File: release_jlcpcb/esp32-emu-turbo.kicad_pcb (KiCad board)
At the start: 4 copper layers, 160 x 75 mm, 71 parts, among them J1 USB-C-16P, J3 JST-PH-2P, J4 FPC-40P-0.5mm, SW1 SW-SMD-5.1x5.1, SW10 SW-SMD-5.1x5.1, SW11 SW-SMD-5.1x5.1, SW12 SW-SMD-5.1x5.1, SW13 SW-SMD-5.1x5.1, SW2 SW-SMD-5.1x5.1, SW3 SW-SMD-5.1x5.1, SW4 SW-SMD-5.1x5.1, SW5 SW-SMD-5.1x5.1, SW6 SW-SMD-5.1x5.1, SW7 SW-SMD-5.1x5.1, SW8 SW-SMD-5.1x5.1, SW9 SW-SMD-5.1x5.1, U1 ESP32-S3-WROOM-1-N16R8, U2 ESOP-8, U3 SOT-223, U5 SOP-16, U6 TF-01A

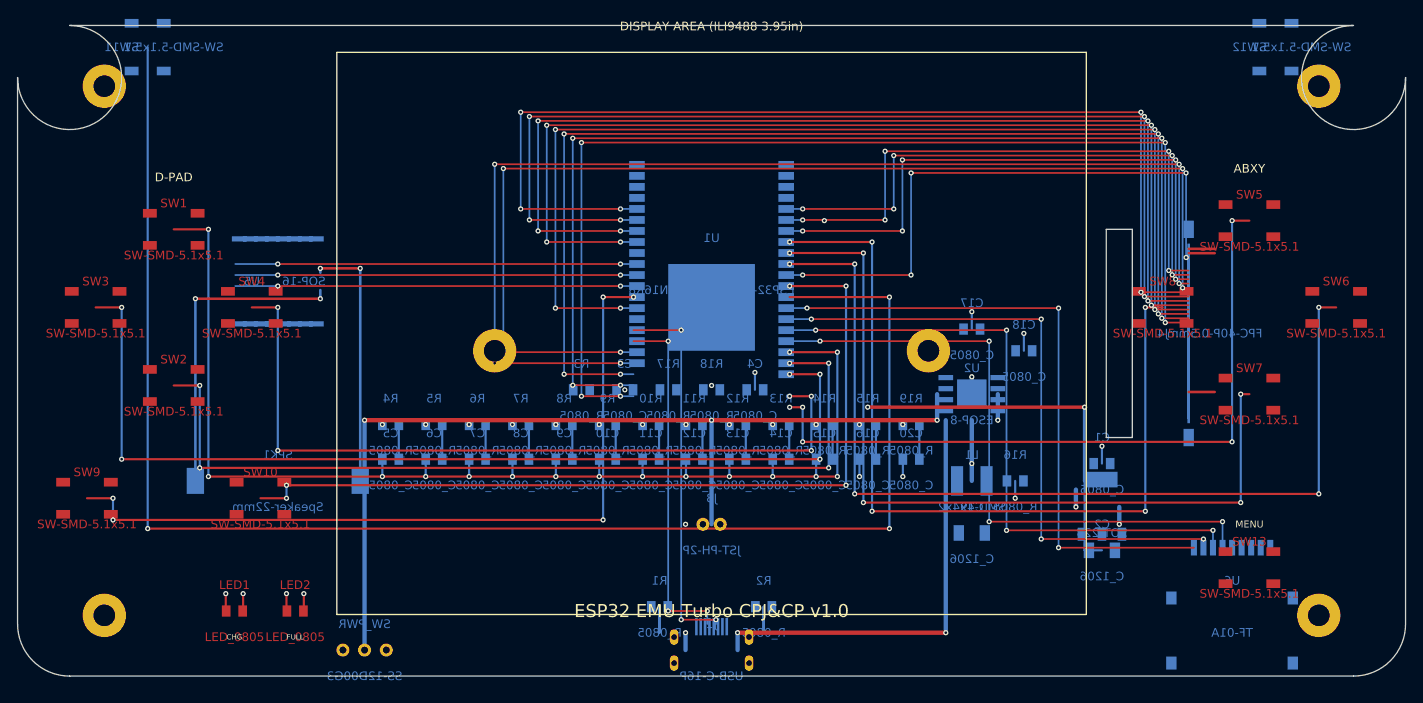
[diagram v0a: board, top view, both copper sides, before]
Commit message: Fix text on copper layers, add DRC check, regenerate JLCPCB files
- Move all Reference/Value text from F.Cu/B.Cu to F.SilkS/B.SilkS
  in PCB generator (board.py) — fixes 130 text-on-copper issues
- Add "Text on Copper Layers" check to drc_check.py (blocks commit
  if any property text is placed on copper layers)
- Regenerate Gerbers, CPL, and gerbers.zip with KiCad 10 (nightly)
- Re-render all 4 PCB 3D views + GLB + 2D SVGs with corrected layers
- Update release_jlcpcb/ folder with fresh exports

Co-Authored-By: Claude Opus 4.6 <noreply@anthropic.com>
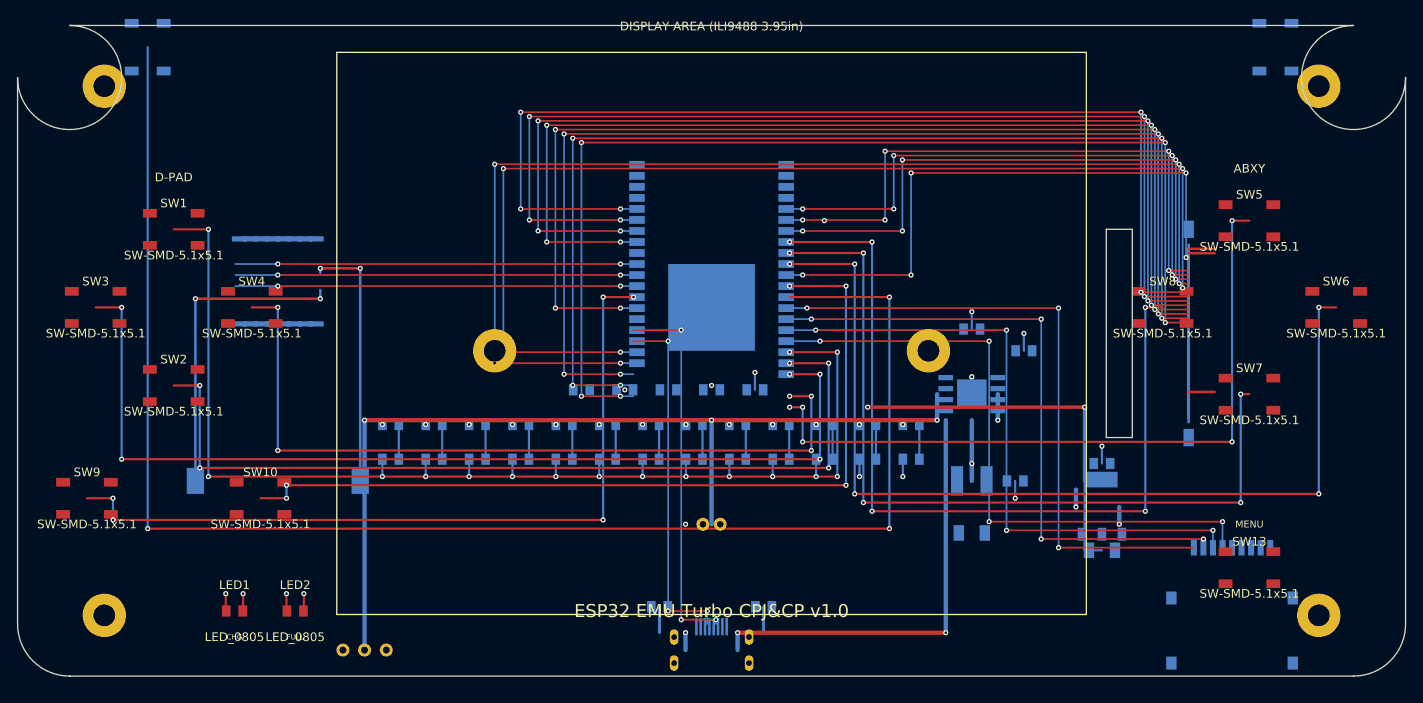
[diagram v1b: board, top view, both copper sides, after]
